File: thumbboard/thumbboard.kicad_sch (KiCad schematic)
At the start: 5 parts, among them J1 Conn_01x05_MountingPin, SW1 SW_Push, SW2 SW_Push, SW3 SW_Push, SW4 SW_Push

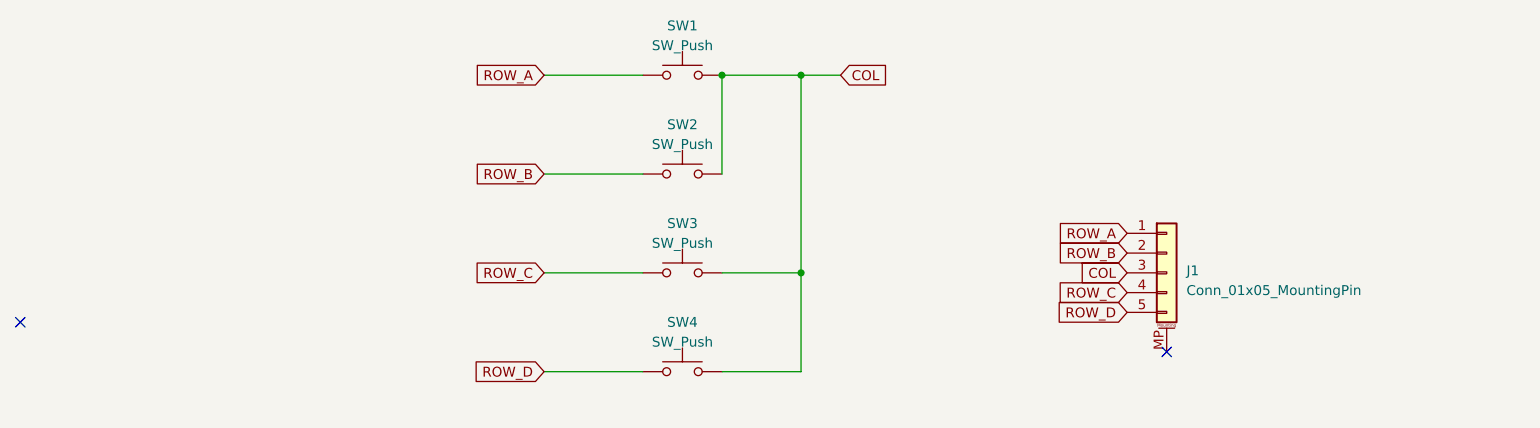
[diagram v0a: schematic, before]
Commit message: complete thumbboard; increase arclength and sharpen angle
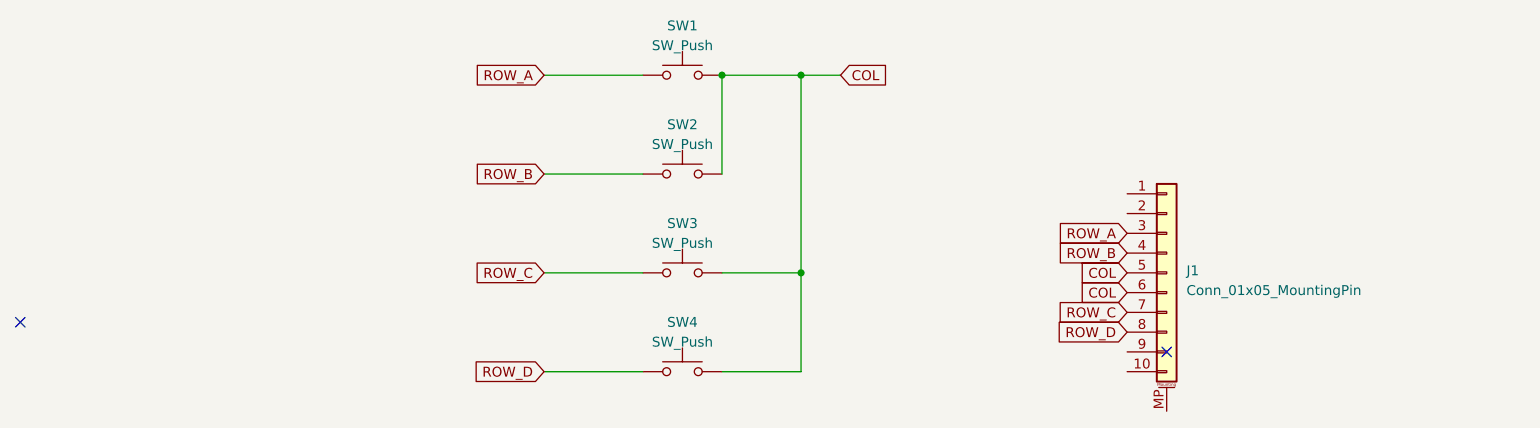
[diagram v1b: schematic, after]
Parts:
- J1: footprint Connector_FFC-FPC:TE_84952-5_1x05-1MP_P1.0mm_Horizontal -> Custom:FFC_Clamshell_0.5mm_1x10; symbol Connector_Generic_MountingPin:Conn_01x05_MountingPin -> Connector_Generic_MountingPin:Conn_01x10_MountingPin
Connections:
- net COL: now also J1.5 (Pin_5), J1.6 (Pin_6), SW1.2, SW3.2; no longer J1.3 (Pin_3), SW1.1, SW3.1
- net ROW_A: now also J1.3 (Pin_3), SW1.1; no longer J1.1 (Pin_1), SW1.2
- net ROW_B: now also J1.4 (Pin_4); no longer J1.2 (Pin_2)
- net ROW_C: now also J1.7 (Pin_7), SW3.1; no longer J1.4 (Pin_4), SW3.2
- net ROW_D: now also J1.8 (Pin_8); no longer J1.5 (Pin_5)
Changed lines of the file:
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@@
     (stroke (width 0) (type default))
   )
-  (global_label "ROW_D" (shape input) (at 163.83 119.38 180) (fields_autoplaced)
+  (global_label "ROW_D" (shape input) (at 163.83 121.92 180) (fields_autoplaced)
     (effects (font (size 1.27 1.27)) (justify right))
-    (property "Intersheetrefs" "${INTERSHEET_REFS}" (at 154.6347 119.38 0)
+    (property "Intersheetrefs" "${INTERSHEET_REFS}" (at 154.6347 121.92 0)
       (effects (font (size 1.27 1.27)) (justify right) hide)
     )
@@
     )
   )
+  (global_label "COL" (shape input) (at 163.83 116.84 180) (fields_autoplaced)
+    (effects (font (size 1.27 1.27)) (justify right))
+    (property "Intersheetrefs" "${INTERSHEET_REFS}" (at 157.2956 116.84 0)
+      (effects (font (size 1.27 1.27)) (justify right) hide)
+    )
+  )
   (global_label "ROW_A" (shape input) (at 88.9 88.9 180) (fields_autoplaced)
     (effects (font (size 1.27 1.27)) (justify right))
@@
     )
   )
-  (global_label "ROW_C" (shape input) (at 163.83 116.84 180) (fields_autoplaced)
+  (global_label "ROW_C" (shape input) (at 163.83 119.38 180) (fields_autoplaced)
     (effects (font (size 1.27 1.27)) (justify right))
-    (property "Intersheetrefs" "${INTERSHEET_REFS}" (at 154.6347 116.84 0)
+    (property "Intersheetrefs" "${INTERSHEET_REFS}" (at 154.6347 119.38 0)
       (effects (font (size 1.27 1.27)) (justify right) hide)
     )
@@
     )
   )
-  (symbol (lib_id "Switch:SW_Push") (at 106.68 114.3 0) (mirror y) (unit 1)
+  (symbol (lib_id "Switch:SW_Push") (at 106.68 114.3 0) (unit 1)
     (in_bom yes) (on_board yes) (dnp no)
     (property "Reference" "SW3" (at 106.68 107.95 0)
@@
     )
   )
-  (symbol (lib_id "Connector_Generic_MountingPin:Conn_01x05_MountingPin") (at 168.91 114.3 0) (unit 1)
+  (symbol (lib_id "Connector_Generic_MountingPin:Conn_01x10_MountingPin") (at 168.91 114.3 0) (unit 1)
     (in_bom yes) (on_board yes) (dnp no)
     (property "Reference" "J1" (at 171.45 114.0206 0)
@@
       (effects (font (size 1.27 1.27)) (justify left))
     )
-    (property "Footprint" "Connector_FFC-FPC:TE_84952-5_1x05-1MP_P1.0mm_Horizontal" (at 168.91 114.3 0)
+    (property "Footprint" "Custom:FFC_Clamshell_0.5mm_1x10" (at 168.91 114.3 0)
       (effects (font (size 1.27 1.27)) hide)
     )
@@
     )
     (pin "1")
+    (pin "10")
     (pin "2")
     (pin "3")
     (pin "4")
     (pin "5")
+    (pin "6")
+    (pin "7")
+    (pin "8")
+    (pin "9")
     (pin "MP")
     (instances
@@
     )
   )
-  (symbol (lib_id "Switch:SW_Push") (at 106.68 88.9 0) (mirror y) (unit 1)
+  (symbol (lib_id "Switch:SW_Push") (at 106.68 88.9 0) (unit 1)
     (in_bom yes) (on_board yes) (dnp no)
     (property "Reference" "SW1" (at 106.68 82.55 0)

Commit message: Make thumbboard reversible; move connector
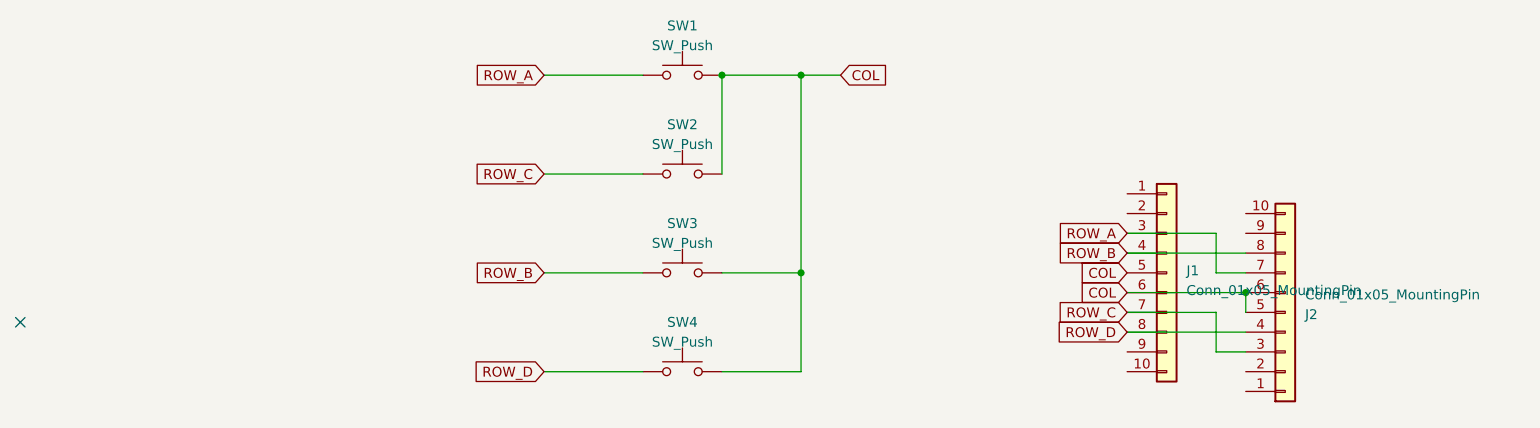
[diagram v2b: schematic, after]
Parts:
- added J2: Conn_01x05_MountingPin, Custom:GCT_FFC2A33-10-T-R_REVA_Clipped2, symbol Connector_Generic:Conn_01x10
- J1: footprint Custom:FFC_Clamshell_0.5mm_1x10 -> Custom:GCT_FFC2A33-10-T-R_REVA_Clipped1; symbol Connector_Generic_MountingPin:Conn_01x10_MountingPin -> Connector_Generic:Conn_01x10
- SW1, SW3, SW4: footprint keyswitches:SW_PG1350 -> keyswitches:SW_PG1350_reversible
- SW2: footprint keyswitches:SW_PG1350 -> keyswitches:SW_PG1350_reversible_MissingCorner
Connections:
- net COL: now also SW1.1, SW3.1, SW4.2, J2.5 (Pin_5), J2.6 (Pin_6); no longer SW1.2, SW3.2, SW4.1
- net ROW_A: now also SW1.2, J2.7 (Pin_7); no longer SW1.1
- net ROW_B: now also SW3.2, J2.8 (Pin_8); no longer SW2.2
- net ROW_C: now also SW2.2, J2.3 (Pin_3); no longer SW3.1
- net ROW_D: now also SW4.1, J2.4 (Pin_4); no longer SW4.2
- no-connect marks 2 -> 1
